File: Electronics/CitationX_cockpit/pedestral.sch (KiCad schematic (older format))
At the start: 30 parts, among them J29 Screw_Terminal_01x10, U31 74HC165, U32 PCF8575, U33 74HC4051

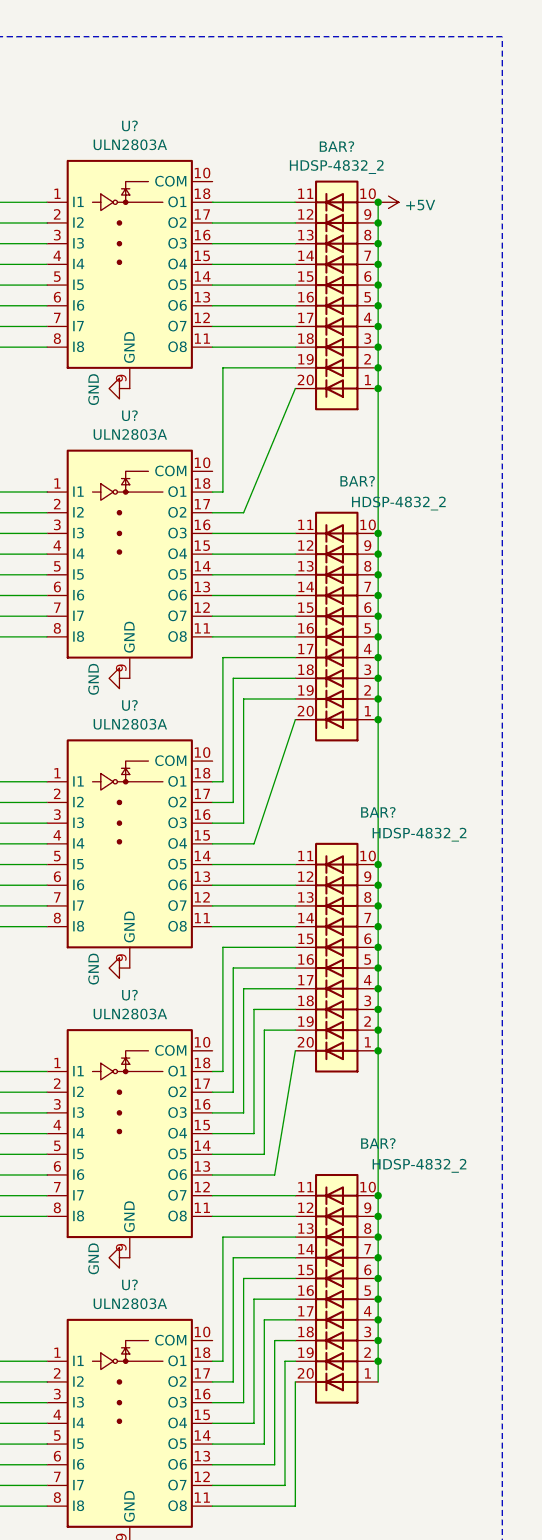
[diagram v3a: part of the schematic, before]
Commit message: Electronics - Added resistor array to limit current in led in pedestral
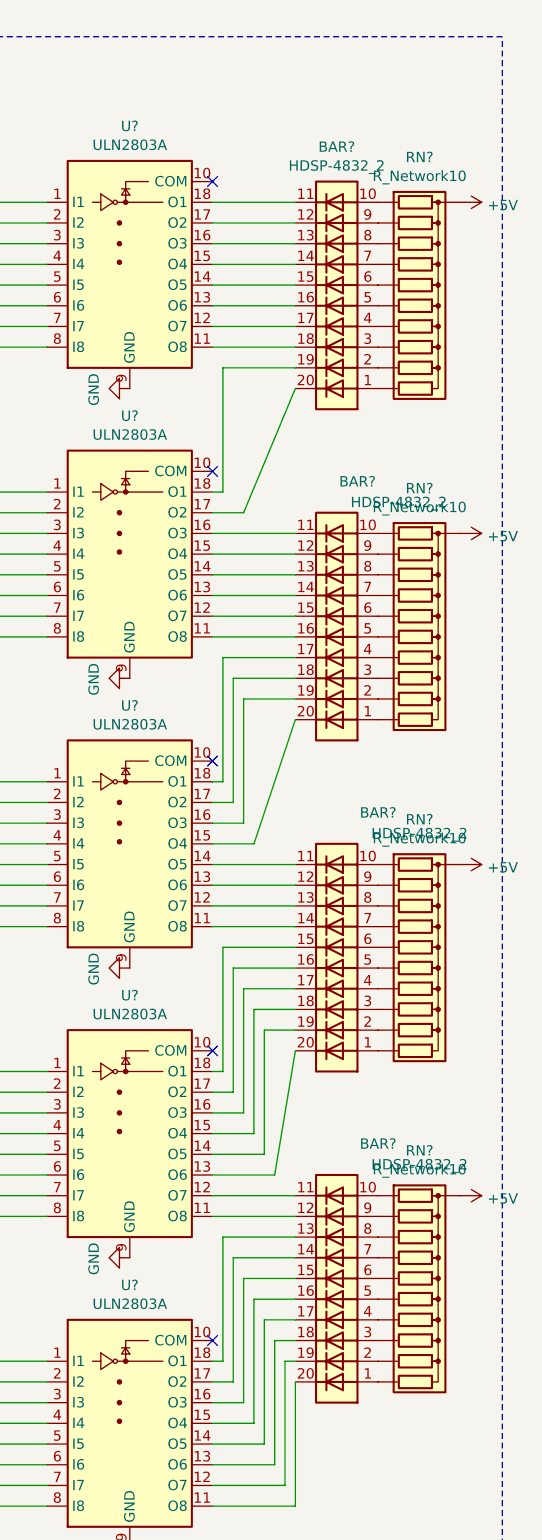
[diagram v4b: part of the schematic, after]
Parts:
- added RN? (x4): R_Network10, Resistor_THT:R_Array_SIP11, symbol Device:R_Network10
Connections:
- net +5V: now also RN?.1 (common), RN?.1 (common), RN?.1 (common), RN?.1 (common); no longer BAR?.1 (A), BAR?.1 (A), BAR?.1 (A), BAR?.1 (A), BAR?.10 (A), BAR?.10 (A), BAR?.10 (A), BAR?.10 (A), BAR?.2 (A), BAR?.2 (A), BAR?.2 (A), BAR?.2 (A), BAR?.3 (A), BAR?.3 (A), BAR?.3 (A), BAR?.3 (A), BAR?.4 (A), BAR?.4 (A), BAR?.4 (A), BAR?.4 (A), BAR?.5 (A), BAR?.5 (A), BAR?.5 (A), BAR?.5 (A), BAR?.6 (A), BAR?.6 (A), BAR?.6 (A), BAR?.6 (A), BAR?.7 (A), BAR?.7 (A), BAR?.7 (A), BAR?.7 (A), BAR?.8 (A), BAR?.8 (A), BAR?.8 (A), BAR?.8 (A), BAR?.9 (A), BAR?.9 (A), BAR?.9 (A), BAR?.9 (A)
- new net: BAR?.1 (A), RN?.11 (R10) (x4)
- new net: BAR?.10 (A), RN?.2 (R1) (x4)
- new net: BAR?.2 (A), RN?.10 (R9) (x4)
- new net: BAR?.3 (A), RN?.9 (R8) (x4)
- new net: BAR?.4 (A), RN?.8 (R7) (x4)
- new net: BAR?.5 (A), RN?.7 (R6) (x4)
- new net: BAR?.6 (A), RN?.6 (R5) (x4)
- new net: BAR?.7 (A), RN?.5 (R4) (x4)
- new net: BAR?.8 (A), RN?.4 (R3) (x4)
- new net: BAR?.9 (A), RN?.3 (R2) (x4)
- no-connect marks 2 -> 7
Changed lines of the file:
@@
 Text Label 4800 2550 0    50   ~ 0
 RUD_TRIM_DT
-$Comp
-L LED:HDSP-4832_2 BAR?
-U 1 1 5DE317D1
-P 16900 9200
-F 0 "BAR?" H 16700 8450 50  0000 C CNN
-F 1 "HDSP-4832_2" H 16500 8550 50  0000 C CNN
-F 2 "Display:HDSP-4832" H 16900 8400 50  0001 C CNN
-F 3 "https://docs.broadcom.com/docs/AV02-1798EN" H 14900 9400 50  0001 C CNN
-	1    16900 9200
-	-1   0    0    1
-$EndComp
 Text HLabel 2250 6450 0    50   Input ~ 0
 ISR_LATCH
@@
 Wire Wire Line
 	16550 9500 16700 9500
-$Comp
-L LED:HDSP-4832_2 BAR?
-U 1 1 5DE755E9
-P 16900 10800
-F 0 "BAR?" H 16700 10050 50  0000 C CNN
-F 1 "HDSP-4832_2" H 16500 10150 50  0000 C CNN
-F 2 "Display:HDSP-4832" H 16900 10000 50  0001 C CNN
-F 3 "https://docs.broadcom.com/docs/AV02-1798EN" H 14900 11000 50  0001 C CNN
-	1    16900 10800
-	-1   0    0    1
-$EndComp
 Wire Wire Line
 	16300 10200 16600 10200
@@
 	-1   0    0    1
 $EndComp
-Wire Wire Line
-	17100 5500 17100 5600
-Wire Wire Line
-	17100 5600 17100 5700
-Connection ~ 17100 5600
-Wire Wire Line
-	17100 5700 17100 5800
-Connection ~ 17100 5700
-Wire Wire Line
-	17100 5800 17100 5900
-Connection ~ 17100 5800
-Wire Wire Line
-	17100 5900 17100 6000
-Connection ~ 17100 5900
-Wire Wire Line
-	17100 6000 17100 6100
-Connection ~ 17100 6000
-Wire Wire Line
-	17100 6100 17100 6200
-Connection ~ 17100 6100
-Wire Wire Line
-	17100 6200 17100 6300
-Connection ~ 17100 6200
-Wire Wire Line
-	17100 6300 17100 6400
-Connection ~ 17100 6300
-Wire Wire Line
-	17100 6400 17100 7100
-Connection ~ 17100 6400
-Wire Wire Line
-	17100 7100 17100 7200
-Connection ~ 17100 7100
-Wire Wire Line
-	17100 7200 17100 7300
-Connection ~ 17100 7200
-Wire Wire Line
-	17100 7300 17100 7400
-Connection ~ 17100 7300
-Wire Wire Line
-	17100 7400 17100 7500
-Connection ~ 17100 7400
-Wire Wire Line
-	17100 7500 17100 7600
-Connection ~ 17100 7500
-Wire Wire Line
-	17100 7600 17100 7700
-Connection ~ 17100 7600
-Wire Wire Line
-	17100 7700 17100 7800
-Connection ~ 17100 7700
-Wire Wire Line
-	17100 7800 17100 7900
-Connection ~ 17100 7800
-Wire Wire Line
-	17100 7900 17100 8000
-Connection ~ 17100 7900
-Wire Wire Line
-	17100 8700 17100 8800
-Wire Wire Line
-	17100 8800 17100 8900
-Connection ~ 17100 8800
-Wire Wire Line
-	17100 8900 17100 9000
-Connection ~ 17100 8900
-Wire Wire Line
-	17100 9000 17100 9100
-Connection ~ 17100 9000
-Wire Wire Line
-	17100 9100 17100 9200
-Connection ~ 17100 9100
-Wire Wire Line
-	17100 9200 17100 9300
-Connection ~ 17100 9200
-Wire Wire Line
-	17100 9300 17100 9400
-Connection ~ 17100 9300
-Wire Wire Line
-	17100 9400 17100 9500
-Connection ~ 17100 9400
-Wire Wire Line
-	17100 9500 17100 9600
-Connection ~ 17100 9500
-Wire Wire Line
-	17100 9600 17100 10300
-Connection ~ 17100 9600
-Wire Wire Line
-	17100 10300 17100 10400
-Connection ~ 17100 10300
-Wire Wire Line
-	17100 10400 17100 10500
-Connection ~ 17100 10400
-Wire Wire Line
-	17100 10500 17100 10600
-Connection ~ 17100 10500
-Wire Wire Line
-	17100 10600 17100 10700
-Connection ~ 17100 10600
-Wire Wire Line
-	17100 10700 17100 10800
-Connection ~ 17100 10700
-Wire Wire Line
-	17100 10800 17100 10900
-Connection ~ 17100 10800
-Wire Wire Line
-	17100 10900 17100 11000
-Connection ~ 17100 10900
-Wire Wire Line
-	17100 11000 17100 11100
-Connection ~ 17100 11000
-Wire Wire Line
-	17100 11100 17100 11200
-Connection ~ 17100 11100
-Wire Wire Line
-	17100 8000 17100 8700
-Connection ~ 17100 8000
-Connection ~ 17100 8700
 $Comp
 L power:+5V #PWR?
 U 1 1 5E457D40
-P 17100 5500
-F 0 "#PWR?" H 17100 5350 50  0001 C CNN
-F 1 "+5V" V 17115 5628 50  0000 L CNN
-F 2 "" H 17100 5500 50  0001 C CNN
-F 3 "" H 17100 5500 50  0001 C CNN
-	1    17100 5500
-	0    1    1    0
-$EndComp
-Connection ~ 17100 5500
+P 17500 5500
+F 0 "#PWR?" H 17500 5350 50  0001 C CNN
+F 1 "+5V" V 17515 5628 50  0000 L CNN
+F 2 "" H 17500 5500 50  0001 C CNN
+F 3 "" H 17500 5500 50  0001 C CNN
+	1    17500 5500
+	0    1    1    0
+$EndComp
 Text Notes 11000 11750 0    50   ~ 0
 The LED bars are used for the trim and rudder position display
@@
 Wire Notes Line
 	17700 4700 10100 4700
+$Comp
+L Device:R_Network10 RN?
+U 1 1 5E57E6C3
+P 17300 6000
+F 0 "RN?" V 16583 6000 50  0000 C CNN
+F 1 "R_Network10" V 16674 6000 50  0000 C CNN
+F 2 "Resistor_THT:R_Array_SIP11" V 17875 6000 50  0001 C CNN
+F 3 "http://www.vishay.com/docs/31509/csc.pdf" H 17300 6000 50  0001 C CNN
+	1    17300 6000
+	0    1    1    0
+$EndComp
+$Comp
+L LED:HDSP-4832_2 BAR?
+U 1 1 5DE317D1
+P 16900 9200
+F 0 "BAR?" H 16700 8450 50  0000 C CNN
+F 1 "HDSP-4832_2" H 16500 8550 50  0000 C CNN
+F 2 "Display:HDSP-4832" H 16900 8400 50  0001 C CNN
+F 3 "https://docs.broadcom.com/docs/AV02-1798EN" H 14900 9400 50  0001 C CNN
+	1    16900 9200
+	-1   0    0    1
+$EndComp
+$Comp
+L LED:HDSP-4832_2 BAR?
+U 1 1 5DE755E9
+P 16900 10800
+F 0 "BAR?" H 16700 10050 50  0000 C CNN
+F 1 "HDSP-4832_2" H 16500 10150 50  0000 C CNN
+F 2 "Display:HDSP-4832" H 16900 10000 50  0001 C CNN
+F 3 "https://docs.broadcom.com/docs/AV02-1798EN" H 14900 11000 50  0001 C CNN
+	1    16900 10800
+	-1   0    0    1
+$EndComp
+$Comp
+L Device:R_Network10 RN?
+U 1 1 5E5A2B15
+P 17300 7600
+F 0 "RN?" V 16583 7600 50  0000 C CNN
+F 1 "R_Network10" V 16674 7600 50  0000 C CNN
+F 2 "Resistor_THT:R_Array_SIP11" V 17875 7600 50  0001 C CNN
+F 3 "http://www.vishay.com/docs/31509/csc.pdf" H 17300 7600 50  0001 C CNN
+	1    17300 7600
+	0    1    1    0
+$EndComp
+$Comp
+L Device:R_Network10 RN?
+U 1 1 5E5A3FC7
+P 17300 9200
+F 0 "RN?" V 16583 9200 50  0000 C CNN
+F 1 "R_Network10" V 16674 9200 50  0000 C CNN
+F 2 "Resistor_THT:R_Array_SIP11" V 17875 9200 50  0001 C CNN
+F 3 "http://www.vishay.com/docs/31509/csc.pdf" H 17300 9200 50  0001 C CNN
+	1    17300 9200
+	0    1    1    0
+$EndComp
+$Comp
+L Device:R_Network10 RN?
+U 1 1 5E5A556A
+P 17300 10800
+F 0 "RN?" V 16583 10800 50  0000 C CNN
+F 1 "R_Network10" V 16674 10800 50  0000 C CNN
+F 2 "Resistor_THT:R_Array_SIP11" V 17875 10800 50  0001 C CNN
+F 3 "http://www.vishay.com/docs/31509/csc.pdf" H 17300 10800 50  0001 C CNN
+	1    17300 10800
+	0    1    1    0
+$EndComp
+$Comp
+L power:+5V #PWR?
+U 1 1 5E5AFFF6
+P 17500 7100
+F 0 "#PWR?" H 17500 6950 50  0001 C CNN
+F 1 "+5V" V 17515 7228 50  0000 L CNN
+F 2 "" H 17500 7100 50  0001 C CNN
+F 3 "" H 17500 7100 50  0001 C CNN
+	1    17500 7100
+	0    1    1    0
+$EndComp
+$Comp
+L power:+5V #PWR?
+U 1 1 5E5B0594
+P 17500 8700
+F 0 "#PWR?" H 17500 8550 50  0001 C CNN
+F 1 "+5V" V 17515 8828 50  0000 L CNN
+F 2 "" H 17500 8700 50  0001 C CNN
+F 3 "" H 17500 8700 50  0001 C CNN
+	1    17500 8700
+	0    1    1    0
+$EndComp
+$Comp
+L power:+5V #PWR?
+U 1 1 5E5B0A96
+P 17500 10300
+F 0 "#PWR?" H 17500 10150 50  0001 C CNN
+F 1 "+5V" V 17515 10428 50  0000 L CNN
+F 2 "" H 17500 10300 50  0001 C CNN
+F 3 "" H 17500 10300 50  0001 C CNN
+	1    17500 10300
+	0    1    1    0
+$EndComp
+NoConn ~ 16300 11000
+NoConn ~ 16300 9600
+NoConn ~ 16300 8200
+NoConn ~ 16300 6800
+NoConn ~ 16300 5400
 $EndSCHEMATC

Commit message: Electronics - Misc works
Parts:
- RN? (x4): value R_Network10 -> 150
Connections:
- net GND: now also U?.9 (GND)
- net GND_IDLE_HIGH: now also RN14.4 (R3), U31.4 (D5); no longer RN14.6 (R5), U31.14 (D3)
- net LAND_LIGHT_LH: now also RN?.8 (R7), U?.12 (D1); no longer RN14.4 (R3), U31.4 (D5)
- net LAND_LIGHT_RH: now also RN?.7 (R6), U?.13 (D2); no longer RN14.3 (R2), U31.5 (D6)
- net LH_WING_DN: now also RN?.6 (R5), U?.14 (D3); no longer RN14.2 (R1), U31.6 (D7)
- net PARK_BREAK: now also RN?.4 (R3), U?.4 (D5); no longer RN?.8 (R7), U?.12 (D1)
- net RH_WING_DN: now also RN?.5 (R4), U?.3 (D4); no longer RN?.9 (R8), U?.11 (D0)
- net TAXI_LIGHT: now also RN?.9 (R8), U?.11 (D0); no longer RN14.5 (R4), U31.3 (D4)
- net OSR_X1: now reaches RN?.3 (R2), U?.5 (D6)
- net OSR_X2: now reaches RN?.2 (R1), U?.6 (D7)
- net ISR_OUT: now reaches U?.9 (QH)
- net DIO3 renamed FRICTION
- net S0 renamed A0
- net S1 renamed A1
- net S2 renamed A2
- net SPOILERS renamed SPEEDBRAKE
- net THRUST_L renamed THROTTLE_L
- net THRUST_R renamed THROTTLE_R
- new net ENG_SYNC_FAN: RN14.3 (R2), U31.5 (D6)
- new net ENG_SYNC_TURB: RN14.2 (R1), U31.6 (D7)
- new net REVERSE_LH: RN14.6 (R5), U31.14 (D3)
- new net REVERSE_RH: RN14.5 (R4), U31.3 (D4)
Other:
- note added: "Blue LEDS have are 4V. -> I need 5V\nRest is 2V.\n2V is the worst case scenario I=(Vcc-Vd)/R\nMax I=20mA\nTherefore R = (5-2)/20m = 150 ohms"
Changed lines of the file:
@@
 EESchema Schematic File Version 4
 LIBS:CitationX_cockpit-cache
-EELAYER 30 0
+EELAYER 26 0
 EELAYER END
 $Descr A2 23386 16535
@@
 $EndComp
 Text Label 6900 1250 0    50   ~ 0
-SPOILERS
+SPEEDBRAKE
 Text Label 6900 1350 0    50   ~ 0
-THRUST_L
+THROTTLE_L
 Text Label 6900 1450 0    50   ~ 0
-THRUST_R
+THROTTLE_R
 Text Label 6900 1550 0    50   ~ 0
-DIO3
+FRICTION
 Text Label 6900 1650 0    50   ~ 0
 FLAPS
@@
 Wire Wire Line
 	6300 1050 6500 1050
-Text HLabel 6200 1250 0    50   Output ~ 0
-ADC
 Text HLabel 6200 1850 0    50   Input ~ 0
 ADC_E
-Text HLabel 6200 1450 0    50   Input ~ 0
-S0
-Text HLabel 6200 1550 0    50   Input ~ 0
-S1
-Text HLabel 6200 1650 0    50   Input ~ 0
-S2
 Text HLabel 2250 3400 0    50   Input ~ 0
 ISR_IN
-Text HLabel 2250 4600 0    50   Input ~ 0
-ISR_LATCH
 $Comp
 L pkl_misc:74HC165 U?
@@
 	0    -1   -1   0
 $EndComp
-Text HLabel 2250 4400 0    50   Input ~ 0
-CLK
 NoConn ~ 3450 4400
 Wire Wire Line
@@
 Wire Wire Line
 	1150 4200 1050 4200
-Text Label 2250 3800 2    50   ~ 0
+Text Label 2250 4000 2    50   ~ 0
 GND_IDLE_HIGH
-Text Label 2250 3900 2    50   ~ 0
+Text Label 2250 5350 2    50   ~ 0
 TAXI_LIGHT
-Text Label 2250 4000 2    50   ~ 0
+Text Label 2250 5450 2    50   ~ 0
 LAND_LIGHT_LH
-Text Label 2250 4100 2    50   ~ 0
+Text Label 2250 5550 2    50   ~ 0
 LAND_LIGHT_RH
-Text Label 2250 4200 2    50   ~ 0
+Text Label 2250 5650 2    50   ~ 0
 LH_WING_DN
 Text Label 4800 2450 0    50   ~ 0
@@
 Text Label 4800 2550 0    50   ~ 0
 RUD_TRIM_DT
-Text HLabel 2250 6450 0    50   Input ~ 0
-ISR_LATCH
 $Comp
 L pkl_misc:74HC165 U?
@@
 	0    -1   -1   0
 $EndComp
-Text HLabel 2250 6250 0    50   Input ~ 0
-CLK
 NoConn ~ 3450 6250
-Wire Wire Line
-	3450 6050 3900 6050
 $Comp
 L Device:C_Small C?
@@
 	0    -1   -1   0
 $EndComp
-Text Label 2250 5450 2    50   ~ 0
+Text Label 2250 5850 2    50   ~ 0
 PARK_BREAK
 Wire Wire Line
@@
 Wire Wire Line
 	2250 4900 2250 5250
-Text Label 2250 5350 2    50   ~ 0
+Text Label 2250 5750 2    50   ~ 0
 RH_WING_DN
 $Comp
@@
 P 16900 7600
 F 0 "BAR?" H 16800 6850 50  0000 C CNN
-F 1 "HDSP-4832_2" H 16600 6950 50  0000 C CNN
+F 1 "HDSP-4832_2" H 16950 6950 50  0000 C CNN
 F 2 "Display:HDSP-4832" H 16900 6800 50  0001 C CNN
 F 3 "https://docs.broadcom.com/docs/AV02-1798EN" H 14900 7800 50  0001 C CNN
@@
 Wire Wire Line
 	16350 6900 16300 6900
-Wire Wire Line
-	16700 6400 16450 7000
 Wire Wire Line
 	16450 7000 16300 7000
@@
 	16450 8500 16300 8500
 Wire Wire Line
-	16700 8000 16500 8600
-Wire Wire Line
 	16500 8600 16300 8600
 Wire Wire Line
@@
 Wire Wire Line
 	16300 10200 16600 10200
-Wire Wire Line
-	16600 10200 16700 9600
 Wire Wire Line
 	16700 10300 16300 10300
@@
 	0    1    1    0
 $EndComp
-Text Notes 11000 11750 0    50   ~ 0
+Text Notes 12900 4900 0    50   ~ 0
 The LED bars are used for the trim and rudder position display
 Wire Notes Line
@@
 P 17300 6000
 F 0 "RN?" V 16583 6000 50  0000 C CNN
-F 1 "R_Network10" V 16674 6000 50  0000 C CNN
+F 1 "150" V 16674 6000 50  0000 C CNN
 F 2 "Resistor_THT:R_Array_SIP11" V 17875 6000 50  0001 C CNN
 F 3 "http://www.vishay.com/docs/31509/csc.pdf" H 17300 6000 50  0001 C CNN
@@
 U 1 1 5DE317D1
 P 16900 9200
-F 0 "BAR?" H 16700 8450 50  0000 C CNN
-F 1 "HDSP-4832_2" H 16500 8550 50  0000 C CNN
+F 0 "BAR?" H 16900 8450 50  0000 C CNN
+F 1 "HDSP-4832_2" H 16850 8550 50  0000 C CNN
 F 2 "Display:HDSP-4832" H 16900 8400 50  0001 C CNN
 F 3 "https://docs.broadcom.com/docs/AV02-1798EN" H 14900 9400 50  0001 C CNN
@@
 U 1 1 5DE755E9
 P 16900 10800
-F 0 "BAR?" H 16700 10050 50  0000 C CNN
-F 1 "HDSP-4832_2" H 16500 10150 50  0000 C CNN
+F 0 "BAR?" H 16900 10050 50  0000 C CNN
+F 1 "HDSP-4832_2" H 16900 10150 50  0000 C CNN
 F 2 "Display:HDSP-4832" H 16900 10000 50  0001 C CNN
 F 3 "https://docs.broadcom.com/docs/AV02-1798EN" H 14900 11000 50  0001 C CNN
@@
 P 17300 7600
 F 0 "RN?" V 16583 7600 50  0000 C CNN
-F 1 "R_Network10" V 16674 7600 50  0000 C CNN
+F 1 "150" V 16674 7600 50  0000 C CNN
 F 2 "Resistor_THT:R_Array_SIP11" V 17875 7600 50  0001 C CNN
 F 3 "http://www.vishay.com/docs/31509/csc.pdf" H 17300 7600 50  0001 C CNN
@@
 P 17300 9200
 F 0 "RN?" V 16583 9200 50  0000 C CNN
-F 1 "R_Network10" V 16674 9200 50  0000 C CNN
+F 1 "150" V 16674 9200 50  0000 C CNN
 F 2 "Resistor_THT:R_Array_SIP11" V 17875 9200 50  0001 C CNN
 F 3 "http://www.vishay.com/docs/31509/csc.pdf" H 17300 9200 50  0001 C CNN
@@
 P 17300 10800
 F 0 "RN?" V 16583 10800 50  0000 C CNN
-F 1 "R_Network10" V 16674 10800 50  0000 C CNN
+F 1 "150" V 16674 10800 50  0000 C CNN
 F 2 "Resistor_THT:R_Array_SIP11" V 17875 10800 50  0001 C CNN
 F 3 "http://www.vishay.com/docs/31509/csc.pdf" H 17300 10800 50  0001 C CNN
@@
 NoConn ~ 16300 6800
 NoConn ~ 16300 5400
+Text Notes 18050 6000 0    50   ~ 0
+Blue LEDS have are 4V. -> I need 5V\nRest is 2V.\n2V is the worst case scenario I=(Vcc-Vd)/R\nMax I=20mA\nTherefore R = (5-2)/20m = 150 ohms
+Wire Wire Line
+	16450 7000 16450 6400
+Wire Wire Line
+	16450 6400 16700 6400
+Wire Wire Line
+	16500 8600 16500 8000
+Wire Wire Line
+	16500 8000 16700 8000
+Wire Wire Line
+	16600 10200 16600 9600
+Wire Wire Line
+	16600 9600 16700 9600
+$Comp
+L power:GND #PWR?
+U 1 1 5DE53801
+P 15900 12000
+AR Path="/5DB5DCD1/5DE53801" Ref="#PWR?"  Part="1"
+AR Path="/5DC174D4/5DE53801" Ref="#PWR?"  Part="1"
+AR Path="/5DBF6FEB/5DE53801" Ref="#PWR?"  Part="1"
+F 0 "#PWR?" H 15900 11750 50  0001 C CNN
+F 1 "GND" H 15905 11827 50  0000 C CNN
+F 2 "" H 15900 12000 50  0001 C CNN
+F 3 "" H 15900 12000 50  0001 C CNN
+	1    15900 12000
+	0    1    1    0
+$EndComp
+Text Label 2250 4200 2    50   ~ 0
+ENG_SYNC_TURB
+Text Label 2250 4100 2    50   ~ 0
+ENG_SYNC_FAN
+Text Label 2250 3800 2    50   ~ 0
+REVERSE_LH
+Text Label 2250 3900 2    50   ~ 0
+REVERSE_RH
+Text Label 2250 5950 2    50   ~ 0
+OSR_X1
+Text Label 2250 6050 2    50   ~ 0
+OSR_X2
+Text HLabel 3450 6050 2    50   Input ~ 0
+ISR_OUT
+Text GLabel 6200 1250 0    50   Output ~ 0
+ADC
+Text GLabel 6200 1550 0    50   Input ~ 0
+A1
+Text GLabel 6200 1650 0    50   Input ~ 0
+A2
+Text GLabel 6200 1450 0    50   Input ~ 0
+A0
+Text GLabel 2250 4600 0    50   Input ~ 0
+ISR_LATCH
+Text GLabel 2250 6450 0    50   Input ~ 0
+ISR_LATCH
+Text GLabel 2250 6250 0    50   Input ~ 0
+CLK
+Text GLabel 2250 4400 0    50   Input ~ 0
+CLK
 $EndSCHEMATC

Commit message: Electronics - Moved library to root of Electronics
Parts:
- added U?: ProMicro, symbol promicro:ProMicro
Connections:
- net A0: now also U?.7 (D4/A6)
- net A1: now also U?.8 (D5)
- net A2: now also U?.9 (D6/A7)
- net ADC_E: now also U?.10 (D7)
- net INT: now also U?.11 (D8/A8)
- net SCL: now also U?.6 (D3/SCL)
- net SDA: now also U?.5 (D2/SDA)
- new net RX: U?.1 (D1/TX)
- new net TX: U?.2 (D0/RX)
- no-connect marks 7 -> 9
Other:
- moved on the sheet: BAR?, C?, RN?, U?
